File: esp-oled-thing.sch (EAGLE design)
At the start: 19 parts, among them IC1 REG1117

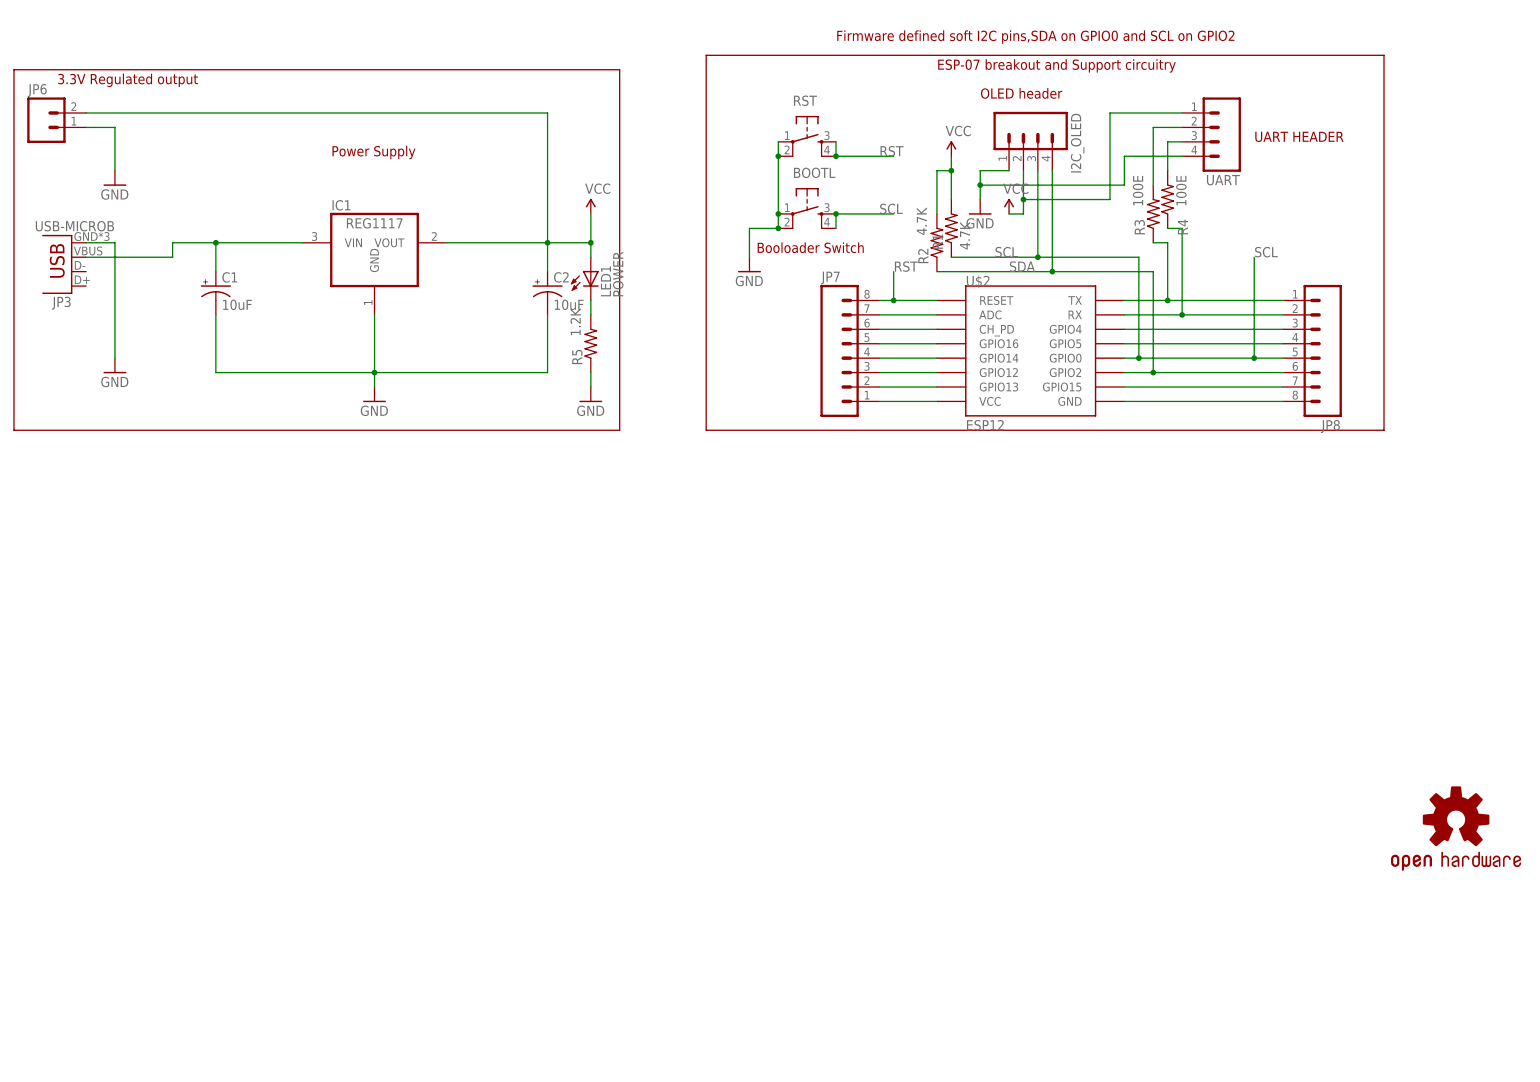
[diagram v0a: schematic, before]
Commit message: tps61200 and mcp73831 for better lipo battery support added, usb connector changed to a more sturdier form factor
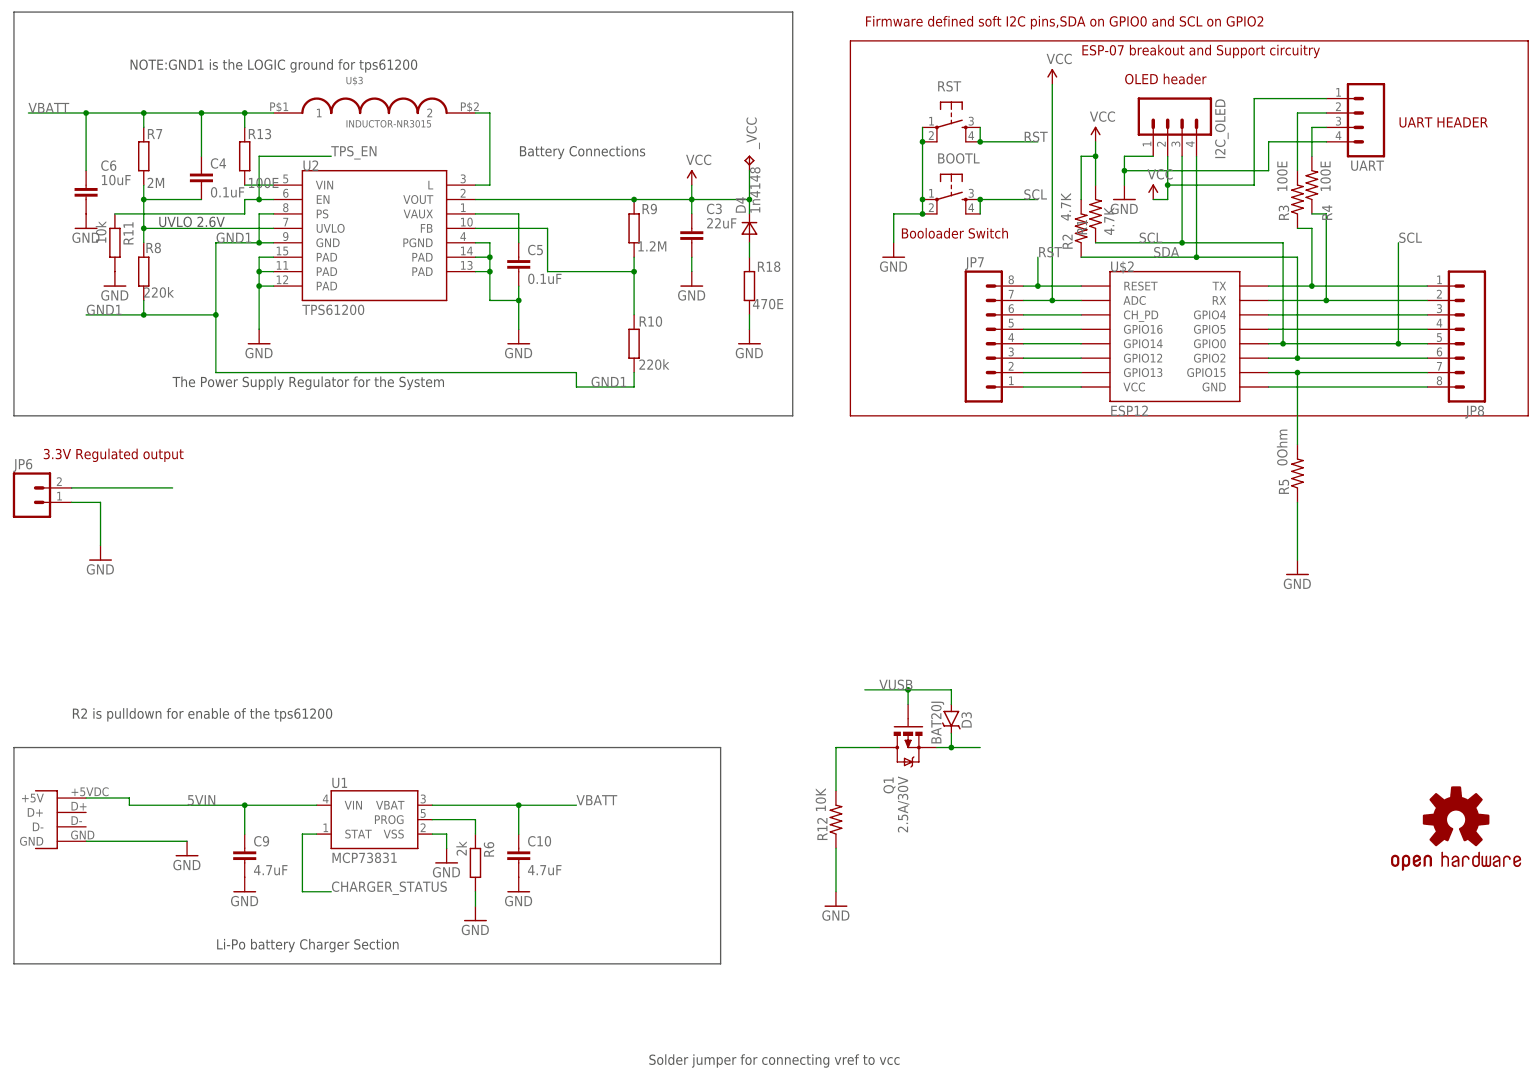
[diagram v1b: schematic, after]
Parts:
- removed C1, C2: 10uF, SparkFun-Capacitors:10UF-16V-10%(TANT)
- removed IC1: REG1117, burr-brown:REG1117
- removed JP3: USB-MICROB, SparkFun-Connectors:USB-MICROB
- removed LED1: POWER, adafruit:LEDCHIPLED_0805
- added C10, C9: 4.7uF, rcl:C-EUC0603K
- added C3: 22uF, rcl:C-EUC0603K
- added C4, C5: 0.1uF, rcl:C-EUC0402
- added C6: 10uF, rcl:C-EUC0805
- added D3: BAT20J, SparkFun-DiscreteSemi:DIODE-SCHOTTKY-BAT20J
- added D4: 1n4148, zetex:DSOD323
- added Q1: 2.5A/30V, SparkFun-DiscreteSemi:MOSFET-PCHANNELDMG2307L
- added R10, R8: 220k, rcl:R-EU_R0402
- added R11: 10k, rcl:R-EU_R0402
- added R12: 10K, adafruit:R-US_M0805
- added R13: 100E, rcl:R-EU_R0402
- added R18: 470E, rcl:R-EU_R0402
- added R6: 2k, rcl:R-EU_R0402
- added R7: 2M, rcl:R-EU_R0402
- added R9: 1.2M, rcl:R-EU_R0402
- added U$3: INDUCTOR-NR3015, farasbee:INDUCTOR-NR3015
- added U$4: MICROUSB-MIDMOUNT, farasbee:MICROUSB-MIDMOUNT
- added U1: MCP73831, SparkFun:MCP73831
- added U2: TPS61200, SparkFun:TPS61200
- added _VCC: TPTP10R, testpad:TPTP10R
- R5: value 1.2K -> 0Ohm
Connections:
- removed net N$1: C1.+, IC1.VIN, JP3.VBUS
- removed net N$10: LED1.C, R5.2
- removed net N$3: JP7.7, U$2.ADC
- new net 5VIN: C9.1, U$4.+5V, U1.VIN
- new net CHARGER_STATUS: U1.STAT
- new net FB: R10.2, R9.1, U2.FB
- new net GND1: R10.1, R8.1, U2.GND, U2.PS
- new net N$13: R6.1, U1.PROG
- new net N$14: U$3.2, U2.L
- new net N$18: C5.1, U2.VAUX
- new net N$21: D4.A, R18.2
- new net TPS_EN: R11.1, U2.EN
- new net UVLO: C4.2, R7.1, R8.2, U2.UVLO
- new net VBAT: JP6.2, Q1.D, R12.2
- new net VBATT: C10.1, C4.1, C6.1, R13.2, R7.2, U$3.1, U1.VBAT
- new net VIN: R13.1, U2.VIN
- new net VIN1: D3.C, Q1.S
- new net VUSB: D3.A, Q1.G
- net GND: now also C10.2, C3.2, C5.2, C6.2, C9.2, R11.2, R12.1, R18.1, R6.2, U$4.GND, U1.VSS, U2.PAD@1, U2.PAD@2, U2.PAD@3, U2.PAD@4, U2.PAD@5, U2.PGND; no longer C1.-, C2.-, IC1.GND, JP3.GND
- net N$15: now also R5.2
- net VCC: now also C3.1, D4.C, JP7.7, R9.2, U$2.ADC, U2.VOUT, _VCC.TP; no longer C2.+, IC1.VOUT, JP6.2, LED1.A
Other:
- note added: "Battery Connections"
- note added: "Li-Po battery Charger Section"
- note added: "NOTE:GND1 is the LOGIC ground for tps61200"
- note added: "R2 is pulldown for enable of the tps61200"
- note added: "Solder jumper for connecting vref to vcc"
- note added: "The Power Supply Regulator for the System"
- note added: "UVLO 2.6V"
- note removed: "Power Supply"
- moved on the sheet: BOOTL, I2C_OLED, JP6, JP7, JP8, R1, R2, R3, R4, R5, RST, U$2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
